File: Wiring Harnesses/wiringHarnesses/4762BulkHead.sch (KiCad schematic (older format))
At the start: 12 parts

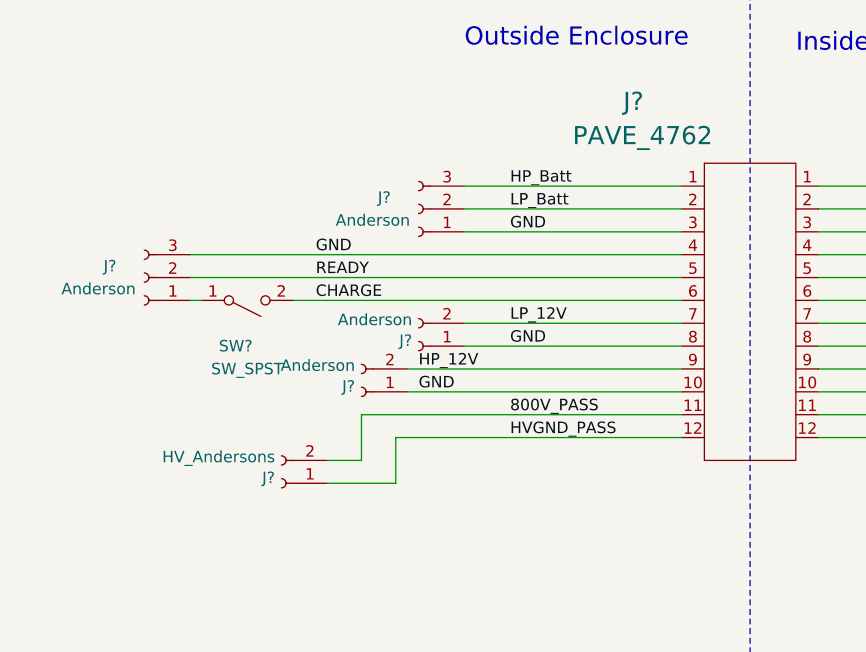
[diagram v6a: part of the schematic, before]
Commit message: Added wire colours to outside connections for 4762 connector.
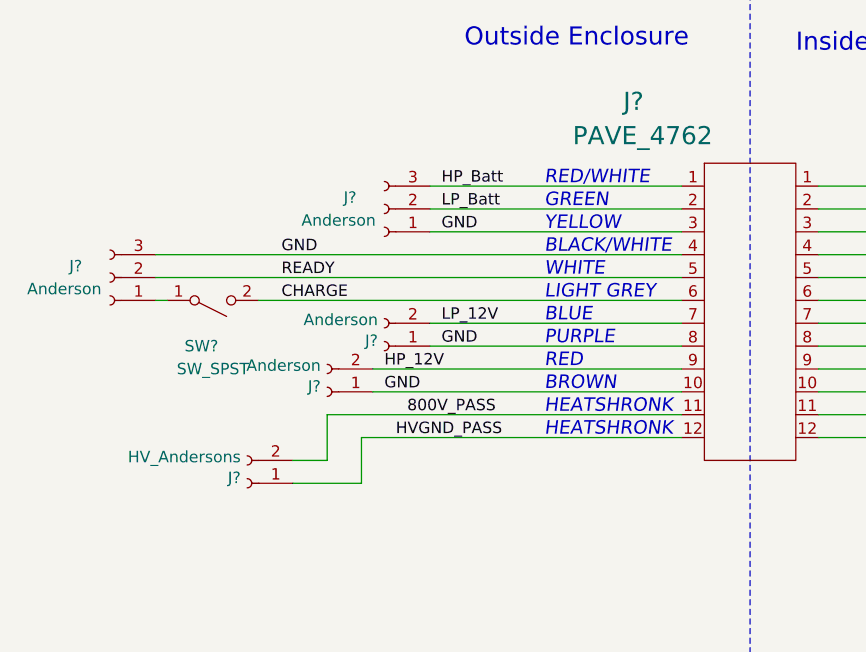
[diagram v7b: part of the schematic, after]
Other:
- note added: "BLACK/WHITE"
- note added: "BLUE"
- note added: "BROWN"
- note added: "GREEN"
- note added: "HEATSHRONK"
- note added: "LIGHT GREY"
- note added: "PURPLE"
- note added: "RED"
- note added: "RED/WHITE"
- note added: "WHITE"
- note added: "YELLOW"
- moved on the sheet: J?, SW?
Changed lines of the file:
@@
 Wire Notes Line
 	5650 1470 5650 6330
-Text Label 4200 4300 0    50   ~ 0
-GND
-Text Label 4200 4200 0    50   ~ 0
+Text Label 4050 4300 0    50   ~ 0
+GND
+Text Label 4050 4200 0    50   ~ 0
 HP_12V
-Text Label 4600 4000 0    50   ~ 0
+Text Label 4300 4000 0    50   ~ 0
 LP_12V
-Text Label 3750 3900 0    50   ~ 0
+Text Label 3600 3900 0    50   ~ 0
 CHARGE
-Text Label 3750 3800 0    50   ~ 0
+Text Label 3600 3800 0    50   ~ 0
 READY
-Text Label 4600 4100 0    50   ~ 0
-GND
-Text Label 4600 4400 0    50   ~ 0
+Text Label 4300 4100 0    50   ~ 0
+GND
+Text Label 4150 4400 0    50   ~ 0
 800V_PASS
-Text Label 4600 4500 0    50   ~ 0
+Text Label 4100 4500 0    50   ~ 0
 HVGND_PASS
 Text Label 7150 4300 2    50   ~ 0
@@
 Text Label 6700 4400 2    50   ~ 0
 800V_PASS
-Text Label 4600 3600 0    50   ~ 0
+Text Label 4300 3600 0    50   ~ 0
 GND
 Text Label 6400 3600 0    50   ~ 0
 GND
-Text Label 3750 3700 0    50   ~ 0
-GND
-Text Label 4600 3500 0    50   ~ 0
+Text Label 3600 3700 0    50   ~ 0
+GND
+Text Label 4300 3500 0    50   ~ 0
 LP_Batt
-Text Label 4600 3400 0    50   ~ 0
+Text Label 4300 3400 0    50   ~ 0
 HP_Batt
 Wire Wire Line
@@
 L Connector:Conn_01x02_Female J?
 U 1 1 5D0C44EB
-P 3950 4300
-F 0 "J?" H 3978 4276 50  0000 L CNN
-F 1 "Anderson" H 3978 4185 50  0000 L CNN
-F 2 "" H 3950 4300 50  0001 C CNN
-F 3 "~" H 3950 4300 50  0001 C CNN
-	1    3950 4300
-	-1   0    0    1
-$EndComp
-Wire Wire Line
-	4150 4200 5350 4200
-Wire Wire Line
-	4150 4300 5350 4300
+P 3800 4300
+F 0 "J?" H 3828 4276 50  0000 L CNN
+F 1 "Anderson" H 3828 4185 50  0000 L CNN
+F 2 "" H 3800 4300 50  0001 C CNN
+F 3 "~" H 3800 4300 50  0001 C CNN
+	1    3800 4300
+	-1   0    0    1
+$EndComp
 $Comp
 L Connector:Conn_01x02_Female J?
 U 1 1 5D0C510C
-P 4200 4100
-F 0 "J?" H 4228 4076 50  0000 L CNN
-F 1 "Anderson" H 4228 3985 50  0000 L CNN
-F 2 "" H 4200 4100 50  0001 C CNN
-F 3 "~" H 4200 4100 50  0001 C CNN
-	1    4200 4100
-	-1   0    0    1
-$EndComp
-Wire Wire Line
-	4400 4100 5350 4100
-Wire Wire Line
-	4400 4000 5350 4000
+P 4050 4100
+F 0 "J?" H 4078 4076 50  0000 L CNN
+F 1 "Anderson" H 4078 3985 50  0000 L CNN
+F 2 "" H 4050 4100 50  0001 C CNN
+F 3 "~" H 4050 4100 50  0001 C CNN
+	1    4050 4100
+	-1   0    0    1
+$EndComp
 $Comp
 L Connector:Conn_01x03_Female J?
 U 1 1 5D0C6DC9
-P 3000 3800
-F 0 "J?" H 3150 3750 50  0000 C CNN
-F 1 "Anderson" H 3200 3850 50  0000 C CNN
-F 2 "" H 3000 3800 50  0001 C CNN
-F 3 "~" H 3000 3800 50  0001 C CNN
-	1    3000 3800
+P 2850 3800
+F 0 "J?" H 3000 3750 50  0000 C CNN
+F 1 "Anderson" H 3050 3850 50  0000 C CNN
+F 2 "" H 2850 3800 50  0001 C CNN
+F 3 "~" H 2850 3800 50  0001 C CNN
+	1    2850 3800
 	-1   0    0    1
 $EndComp
@@
 L Switch:SW_SPST SW?
 U 1 1 5D0C944E
-P 3450 3900
-F 0 "SW?" H 3400 4100 50  0000 C CNN
-F 1 "SW_SPST" H 3450 4200 50  0000 C CNN
-F 2 "" H 3450 3900 50  0001 C CNN
-F 3 "" H 3450 3900 50  0001 C CNN
-	1    3450 3900
-	1    0    0    1
-$EndComp
-Wire Wire Line
-	3200 3900 3250 3900
-Wire Wire Line
-	3650 3900 5350 3900
-Wire Wire Line
-	3200 3800 5350 3800
+P 3300 3900
+F 0 "SW?" H 3250 4100 50  0000 C CNN
+F 1 "SW_SPST" H 3300 4200 50  0000 C CNN
+F 2 "" H 3300 3900 50  0001 C CNN
+F 3 "" H 3300 3900 50  0001 C CNN
+	1    3300 3900
+	1    0    0    1
+$EndComp
+Wire Wire Line
+	3050 3900 3100 3900
 $Comp
 L Connector:Conn_01x03_Female J?
@@
 L Connector:Conn_01x02_Female J?
 U 1 1 5D0D11C4
-P 3600 4700
-F 0 "J?" H 3628 4676 50  0000 L CNN
-F 1 "HV_Andersons" H 3628 4585 50  0000 L CNN
-F 2 "" H 3600 4700 50  0001 C CNN
-F 3 "~" H 3600 4700 50  0001 C CNN
-	1    3600 4700
-	-1   0    0    1
-$EndComp
-Wire Wire Line
-	4100 4500 4100 4700
-Wire Wire Line
-	4100 4700 3800 4700
-Wire Wire Line
-	4100 4500 5350 4500
-Wire Wire Line
-	3800 4600 3950 4600
-Wire Wire Line
-	3950 4600 3950 4400
-Wire Wire Line
-	3950 4400 5350 4400
+P 3450 4700
+F 0 "J?" H 3478 4676 50  0000 L CNN
+F 1 "HV_Andersons" H 3478 4585 50  0000 L CNN
+F 2 "" H 3450 4700 50  0001 C CNN
+F 3 "~" H 3450 4700 50  0001 C CNN
+	1    3450 4700
+	-1   0    0    1
+$EndComp
+Wire Wire Line
+	3950 4500 3950 4700
+Wire Wire Line
+	3950 4700 3650 4700
+Wire Wire Line
+	3650 4600 3800 4600
+Wire Wire Line
+	3800 4600 3800 4400
 $Comp
 L Connector:Conn_01x02_Female J?
@@
 Wire Wire Line
 	5950 4400 7250 4400
-Wire Wire Line
-	5350 3600 4400 3600
-Wire Wire Line
-	4400 3500 5350 3500
-Wire Wire Line
-	4400 3400 5350 3400
 $Comp
 L Connector:Conn_01x03_Female J?
 U 1 1 5D0D8D86
-P 4200 3500
-F 0 "J?" H 4350 3450 50  0000 C CNN
-F 1 "Anderson" H 4400 3550 50  0000 C CNN
-F 2 "" H 4200 3500 50  0001 C CNN
-F 3 "~" H 4200 3500 50  0001 C CNN
-	1    4200 3500
-	-1   0    0    1
-$EndComp
-Wire Wire Line
-	3200 3700 5350 3700
+P 4050 3500
+F 0 "J?" H 4200 3450 50  0000 C CNN
+F 1 "Anderson" H 4250 3550 50  0000 C CNN
+F 2 "" H 4050 3500 50  0001 C CNN
+F 3 "~" H 4050 3500 50  0001 C CNN
+	1    4050 3500
+	-1   0    0    1
+$EndComp
 $Comp
 L Connector:Conn_01x03_Female J?
@@
 Wire Wire Line
 	5950 3700 7350 3700
+Text Notes 4750 3400 0    59   Italic 0
+RED/WHITE
+Text Notes 4750 3500 0    59   Italic 0
+GREEN
+Text Notes 4750 3600 0    59   Italic 0
+YELLOW
+Text Notes 4750 3900 0    59   Italic 0
+LIGHT GREY
+Text Notes 4750 3800 0    59   Italic 0
+WHITE
+Text Notes 4750 3700 0    59   Italic 0
+BLACK/WHITE
+Text Notes 4750 4300 0    59   Italic 0
+BROWN
+Text Notes 4750 4200 0    59   Italic 0
+RED
+Text Notes 4750 4000 0    59   Italic 0
+BLUE
+Text Notes 4750 4100 0    59   Italic 0
+PURPLE
+Text Notes 4750 4400 0    59   Italic 0
+HEATSHRONK
+Text Notes 4750 4500 0    59   Italic 0
+HEATSHRONK
+Wire Wire Line
+	3950 4500 5350 4500
+Wire Wire Line
+	3800 4400 5350 4400
+Wire Wire Line
+	4000 4300 5350 4300
+Wire Wire Line
+	4000 4200 5350 4200
+Wire Wire Line
+	4250 4100 5350 4100
+Wire Wire Line
+	4250 4000 5350 4000
+Wire Wire Line
+	3500 3900 5350 3900
+Wire Wire Line
+	3050 3800 5350 3800
+Wire Wire Line
+	3050 3700 5350 3700
+Wire Wire Line
+	4250 3400 5350 3400
+Wire Wire Line
+	4250 3500 5350 3500
+Wire Wire Line
+	4250 3600 5350 3600
 $EndSCHEMATC

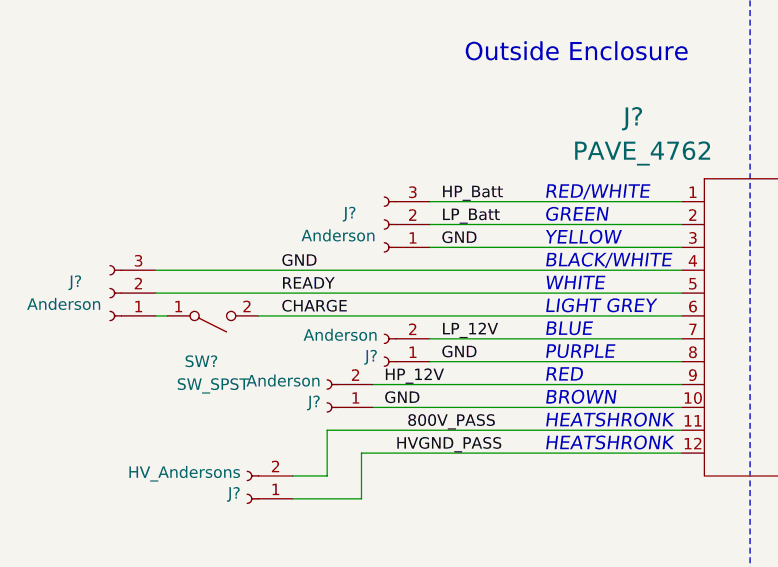
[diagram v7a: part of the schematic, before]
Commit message: Added BMS main i/o  connector picture. To wire later
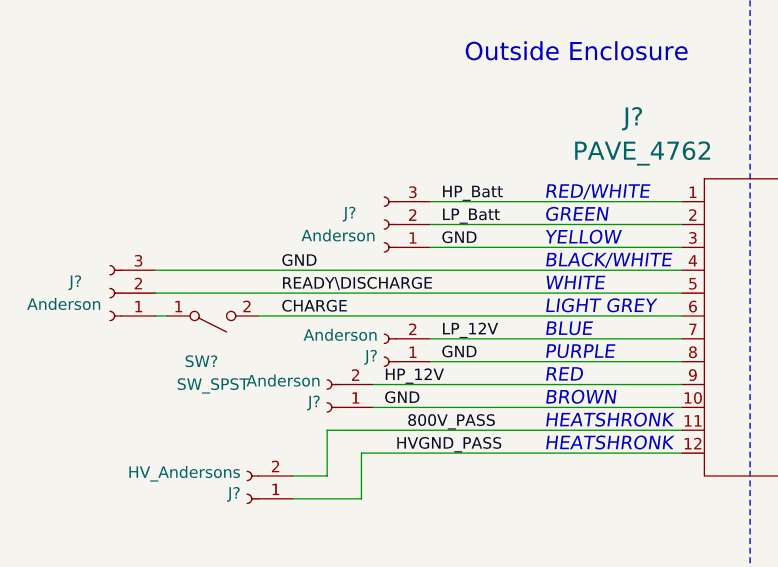
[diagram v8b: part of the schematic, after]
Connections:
- net READY: no longer J?.2 (Pin_2)
- new net READY\DISCHARGE: J?.2 (Pin_2), J?.5
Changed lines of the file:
@@
 CHARGE
 Text Label 3600 3800 0    50   ~ 0
-READY
+READY\DISCHARGE
 Text Label 4300 4100 0    50   ~ 0
 GND
